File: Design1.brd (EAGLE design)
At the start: 60.6 x 59.4 mm, 24 parts, among them U1 ATMEGA328P-AU, X1 +3.3

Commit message: update
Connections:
- net ESP12F(PIN21) renamed RX
- net ESP12F(PIN22) renamed TX
- net N$5 renamed CH_PD
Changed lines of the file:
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@@
 <?xml version="1.0" encoding="utf-8"?>
 <!DOCTYPE eagle SYSTEM "eagle.dtd">
-<eagle version="8.5.2">
+<eagle version="8.7.1">
 <drawing>
 <settings>
@@
 <wire x1="12.45" y1="19.9754" x2="25.92" y2="14.17" width="0" layer="19" extent="1-1"/>
 </signal>
-<signal name="ESP12F(PIN21)">
+<signal name="RX">
 <contactref element="SJ2" pad="1"/>
 <contactref element="MCU_FIRM2" pad="4"/>
@@
 <wire x1="36.52848125" y1="21.999275" x2="53.592815625" y2="53.58893125" width="0" layer="19" extent="1-16"/>
 </signal>
-<signal name="ESP12F(PIN22)">
+<signal name="TX">
 <contactref element="U1" pad="30"/>
 <contactref element="SJ1" pad="1"/>
@@
 <contactref element="U1" pad="11"/>
 </signal>
-<signal name="N$5">
+<signal name="CH_PD">
 <contactref element="U2" pad="3"/>
 </signal>
@@
 </signal>
 </signals>
-<errors>
-</errors>
 </board>
 </drawing>

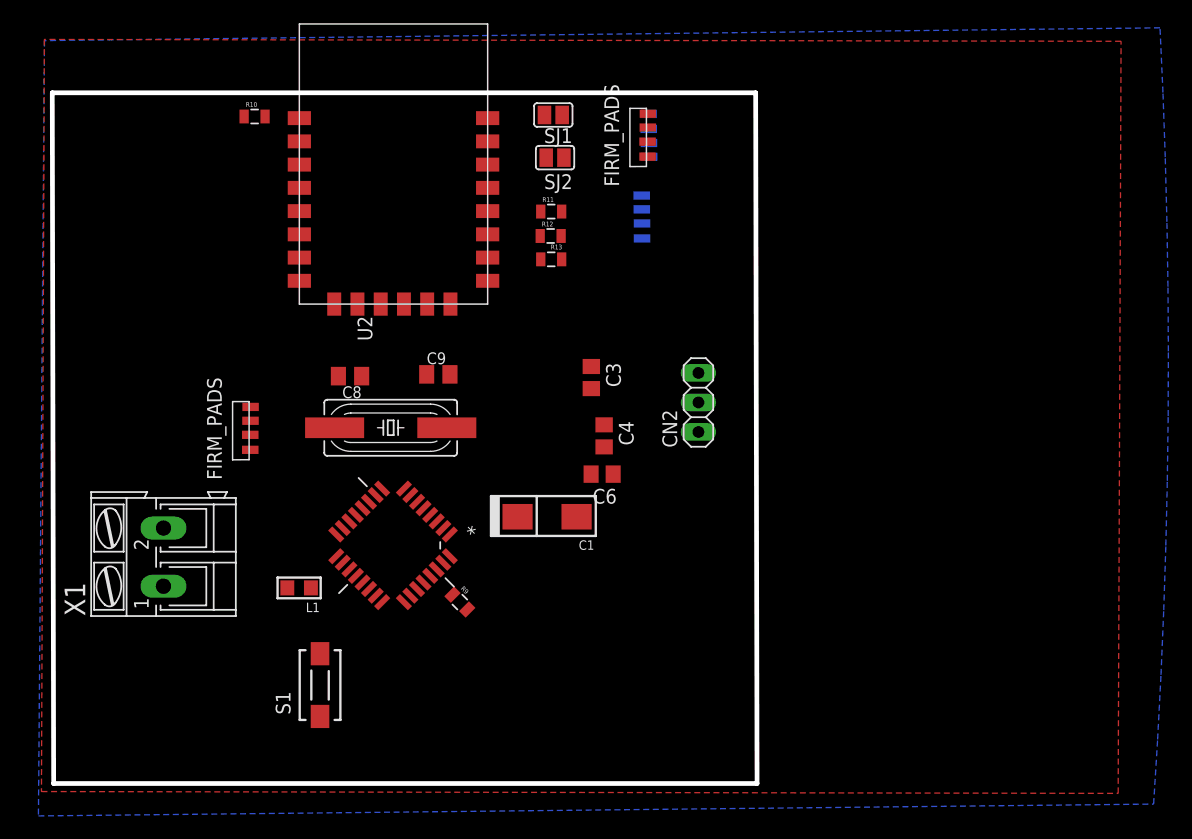
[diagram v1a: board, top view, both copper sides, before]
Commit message: v 0.3 needs location buttons only
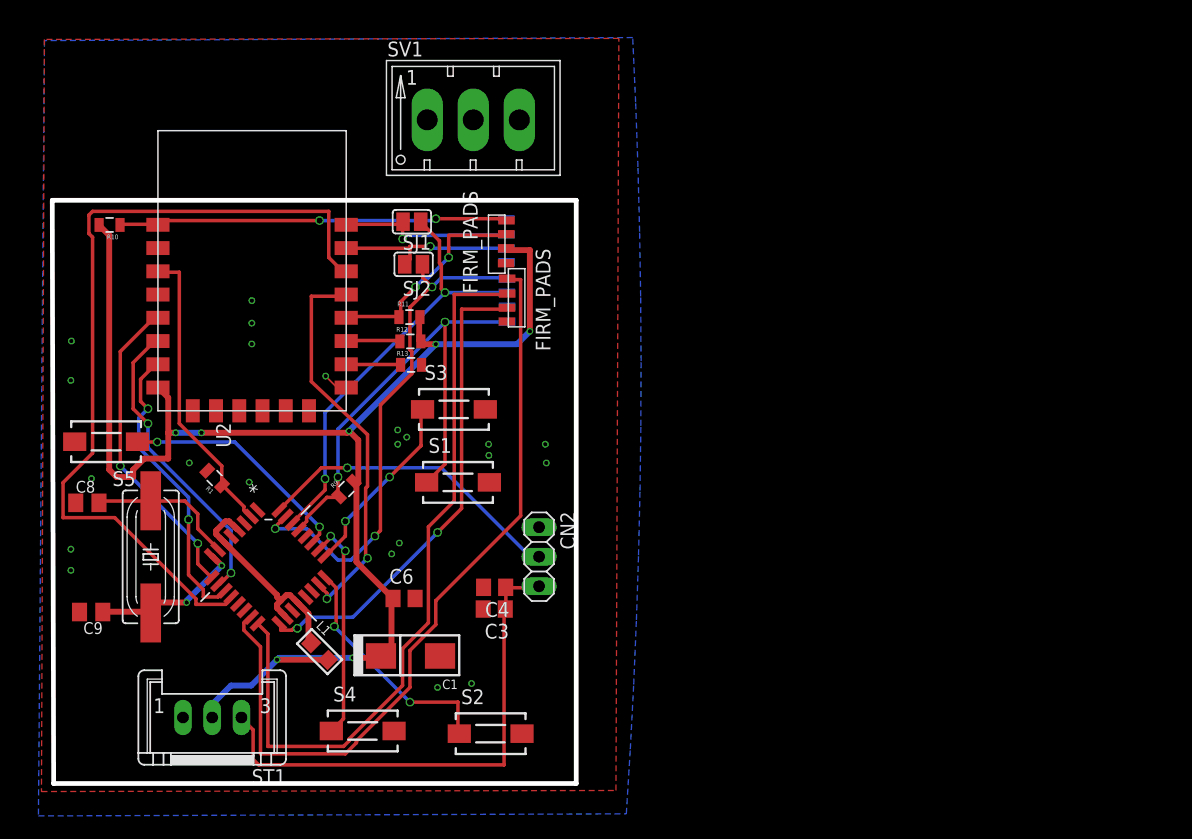
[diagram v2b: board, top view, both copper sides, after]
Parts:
- removed X1: +3.3, con-ptr500:AK300/2
- added R1: 10k, SMD Resistors:0805
- added S2, S3, S4, S5: DTSM-3, switch-tact:DTSM-3
- added ST1: MSF3, con-lumberg:MSF3
- added SV1: (no value), con-amp-mt6:MT6-3Y
- R10: value 10k -> 12K
- moved C9 36.2 mm to (6.22, 17.8), turned to 180 degrees
- moved MCU_FIRM1 27.7 mm to (42.1, 47.3), turned to 270 degrees
- moved C8 25.1 mm to (5.90, 27.1), turned to 0 degrees
- moved OSC1 23.4 mm to (11.3, 22.5), turned to 270 degrees
- moved C3 21.6 mm to (40.9, 18.0), turned to 180 degrees
- moved S1 21.1 mm to (37.8, 28.9), turned to 0 degrees
- moved C6 20.1 mm to (33.1, 18.9), turned to 0 degrees
- moved CN2 19.1 mm to (44.8, 22.5), turned to 270 degrees
- moved C1 16.8 mm to (33.7, 14.0)
- moved C4 16.1 mm to (40.9, 19.9), turned to 180 degrees
- moved R10 15.6 mm to (7.81, 51.1), turned to 180 degrees
- moved U$3 15.3 mm to (41.8, 52.4)
- moved MCU_FIRM3 15.2 mm to (41.8, 46.9)
- moved SJ1 15.2 mm to (33.8, 51.3)
- moved SJ2 15.2 mm to (34.0, 47.7)
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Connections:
- net IRRX renamed MOTION
- removed net +3V1: R9.2
- removed net D/C: U2.13
- removed net N$2: C3.2, C4.2, CN2.1
- removed net RES: U2.14
- removed net SCL: U2.5
- removed net SDA: U2.7
- removed net TEMP: U1.11
- new net 4V5: C3.1, C4.1, CN2.3, ST1.3
- new net BTN_CONFIG: S3.1, U1.25
- new net BTN_RESET: S4.1, U1.26
- new net BTN_TEST: S5.1, U1.27
- new net BTN_UPDATE: S2.1, U1.24
- new net ESP_ACK: U1.12, U2.14
- new net ESP_CONFIG: U1.10, U2.6
- new net ESP_MOTION: U1.9, U2.5
- new net ESP_OK: U1.23, U2.13
- new net ESP_UPDATE: U1.11, U2.7
- new net N$1: MCU_FIRM3.1
- new net N$18: U1.28
- new net N$4: U$3.1
- new net N$8: U1.13
- new net N$9: U1.14
- net +3V3: now also R9.2, ST1.2; no longer C3.1, C4.1, CN2.3, X1.2
- net CH_PD: now also R1.1, U1.2
- net GND: now also C3.2, C4.2, CN2.1, R1.2, S2.2, S3.2, S4.2, S5.2, ST1.1; no longer X1.1
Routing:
- net +3V3: track 0.00 -> 125.5 mm, vias 0 -> 7
- net ESP_ACK: track 0.00 -> 72.1 mm
- net MOSI: track 0.00 -> 68.2 mm
- net MISO: track 0.00 -> 64.9 mm
- net RX: track 0.00 -> 44.8 mm, vias 0 -> 3
- net 4V5: track 0.00 -> 44.0 mm
- net RST_A: track 0.00 -> 43.5 mm, vias 0 -> 2
- net SCK: track 0.00 -> 41.6 mm, vias 0 -> 2
- net TX: track 0.00 -> 37.5 mm, vias 0 -> 2
- net ESP_OK: track 0.00 -> 34.3 mm, vias 0 -> 2
- net RST_E: track 0.00 -> 33.8 mm, vias 0 -> 2
- net ESP_MOTION: track 0.00 -> 27.1 mm, vias 0 -> 2
- net MOTION: track 0.00 -> 27.0 mm, vias 0 -> 1
- net ESP_CONFIG: track 0.00 -> 26.0 mm, vias 0 -> 2
- net ESP_UPDATE: track 0.00 -> 25.9 mm, vias 0 -> 2
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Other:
- board size 60.6 x 59.4 mm -> 45.1 x 50.2 mm

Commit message: v 0.5 good
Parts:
- removed MCU_FIRM1, MCU_FIRM2, MCU_FIRM3, U$3: FIRM_PADSSMD_FIRM_PADS, firm_pads:FIRM_PADS
- added CON1: AT1, firm_pads:FIRM_PADS
- added CON2: AT2, firm_pads:FIRM_PADS
- added CON3: ESP1, firm_pads:FIRM_PADS
- added CON4: ESP2, firm_pads:FIRM_PADS
- S1: value DTSM-3 -> RESET_A
- S2: value DTSM-3 -> UPDATE
- S3: value DTSM-3 -> CONFIG
- S4: value DTSM-3 -> RESET
- S5: value DTSM-3 -> TEST
- moved L1 28.7 mm to (27.5, 43.0), flipped to the bottom, turned to 135 degrees
- moved S3 28.4 mm to (29.3, 7.98)
- moved S5 24.5 mm to (11.0, 8.18)
- moved C9 21.2 mm to (9.08, 38.8), flipped to the bottom, turned to 0 degrees
- moved S2 20.6 mm to (20.0, 8.04)
- moved C1 17.9 mm to (35.3, 31.8), flipped to the bottom, turned to 0 degrees
- moved ST1 16.3 mm to (6.81, 19.2), turned to 90 degrees
- moved U1 14.5 mm to (23.2, 36.0), flipped to the bottom, turned to 135 degrees
- moved S1 14.5 mm to (23.8, 25.2), flipped to the bottom
- moved OSC1 11.8 mm to (14.2, 33.9), flipped to the bottom, turned to 90 degrees
- moved S4 9.06 mm to (38.6, 7.88)
- moved C6 8.63 mm to (35.5, 27.2), flipped to the bottom, turned to 180 degrees
- moved C8 4.10 mm to (9.49, 29.1), flipped to the bottom, turned to 180 degrees
- moved R1 2.28 mm to (19.1, 29.2), flipped to the bottom, turned to 315 degrees
- moved R9 1.62 mm to (28.5, 29.9), flipped to the bottom, turned to 225 degrees
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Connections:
- net N$11 renamed AT_VCC
- removed net N$1: MCU_FIRM3.1
- removed net N$17: MCU_FIRM1.4
- net +3V3: now also CON3.2; no longer MCU_FIRM3.2
- net CH_PD: now also CON3.1
- net GND: now also CON1.4, CON4.4; no longer MCU_FIRM2.2, U$3.4
- net GPIO0: now also CON3.3; no longer MCU_FIRM3.3
- net MISO: now also CON1.2; no longer MCU_FIRM1.2
- net MOSI: now also CON1.1; no longer MCU_FIRM1.1
- net N$4: now also CON4.1; no longer U$3.1
- net RST_A: now also CON2.1; no longer MCU_FIRM2.1
- net RST_E: now also CON3.4; no longer MCU_FIRM3.4
- net RX: now also CON2.4; no longer MCU_FIRM2.4
- net RXD_FIRM: now also CON4.2; no longer U$3.2
- net SCK: now also CON1.3; no longer MCU_FIRM1.3
- net TX: now also CON2.3; no longer MCU_FIRM2.3
- net TXD_FIRM: now also CON4.3; no longer U$3.3
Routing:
- net ESP_ACK: track 72.1 -> 13.3 mm, vias 0 -> 1
- net CH_PD: track 25.5 -> 73.7 mm, vias 0 -> 3
- net MISO: track 64.9 -> 27.4 mm
- net MOSI: track 68.2 -> 31.7 mm, vias 0 -> 2
- net BTN_UPDATE: track 20.8 -> 56.4 mm, vias 2 -> 1
- net SCK: track 41.6 -> 20.8 mm, vias 2 -> 0
- net RST_A: track 43.5 -> 60.1 mm
- net ESP_UPDATE: track 25.9 -> 9.41 mm, vias 2 -> 1
- net ESP_CONFIG: track 26.0 -> 9.77 mm, vias 2 -> 1
- net BTN_TEST: track 20.3 -> 34.2 mm, vias 2 -> 1
- net RX: track 44.8 -> 58.2 mm
- net ESP_OK: track 34.3 -> 21.1 mm, vias 2 -> 1
- net ESP_MOTION: track 27.1 -> 14.3 mm, vias 2 -> 1
- net BTN_CONFIG: track 16.1 -> 28.8 mm, vias 2 -> 1
- net BTN_RESET: track 19.4 -> 30.5 mm, vias 2 -> 1
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
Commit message: v0.6
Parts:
- removed SV1: (no value), con-amp-mt6:MT6-3Y
- added BAT: Bat, jumper:SJ
- added BATL3.3: 3.3, jumper:SJ
- added BATL4.5: 4.5, jumper:SJ
- added CN1: (no value), MicroUSB:USB-MICRO-SMD
- added SG1: F/CM12P, buzzer:F/CM12P
- added U3: LDO, SPX3819M5-L-3-3:SOT95P280X145-5N
- S1, S2, S3, S4, S5: device switch-tact:DTSM-3 -> switch-tact:DTSM-6
- moved S1 21.2 mm to (41.2, 37.3), turned to 180 degrees
- moved S2 20.2 mm to (40.1, 8.79)
- moved C1 15.0 mm to (28.6, 18.3), turned to 270 degrees
- moved S3 14.0 mm to (31.2, 21.9)
- moved S4 9.71 mm to (29.0, 9.00)
- moved C6 8.83 mm to (33.9, 18.5), turned to 90 degrees
- moved S5 7.18 mm to (18.1, 8.99), turned to 0 degrees
- moved ST1 3.56 mm to (4.19, 21.6)
- moved R1 3.54 mm to (22.2, 31.0), turned to 45 degrees
- moved L1 3.27 mm to (30.7, 43.7)
- moved U1 3.13 mm to (26.3, 36.0)
- moved C8 2.94 mm to (12.4, 29.6)
- moved C9 2.84 mm to (11.8, 38.1)
- moved OSC1 2.64 mm to (16.8, 33.5)
- moved R9 2.58 mm to (31.0, 30.5)
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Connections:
- net N$9 renamed SS-
- removed net N$8: U1.13
- new net BAT: BAT.2, BATL3.3.1, ST1.2
- new net BUZZER: SG1.+, U1.13
- new net N$1: BATL3.3.2, BATL4.5.2, CN1.VBUS1, U3.1, U3.3
- net +3V3: now also BAT.1, U3.5; no longer ST1.2
- net 4V5: now also BATL4.5.1
- net GND: now also CN1.GND1, S1.3, S2.3, S3.3, S4.3, S5.3, SG1.-, U3.2; no longer S1.2, S2.2, S3.2, S4.2, S5.2
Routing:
- net BUZZER: track 0.00 -> 83.5 mm, vias 0 -> 1
- net RST_A: track 60.1 -> 27.3 mm, vias 2 -> 0
- net BTN_UPDATE: track 56.4 -> 28.0 mm
- net N$1: track 0.00 -> 25.6 mm, vias 0 -> 2
- net BTN_CONFIG: track 28.8 -> 13.2 mm
- net 4V5: track 40.0 -> 53.5 mm
- net BAT: track 0.00 -> 10.8 mm
- net MOSI: track 31.7 -> 21.5 mm, vias 2 -> 0
- net RX: track 58.2 -> 49.0 mm, vias 3 -> 4
- net MISO: track 27.4 -> 19.4 mm
- net GND: track 0.00 -> 5.97 mm, vias 20 -> 15
- net TX: track 44.1 -> 38.3 mm
- net ESP_UPDATE: track 9.41 -> 13.2 mm
- net SCK: track 20.8 -> 17.1 mm
- net ESP_OK: track 21.1 -> 17.7 mm
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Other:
- board size 45.1 x 50.2 mm -> 45.4 x 50.4 mm

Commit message: v 0.6 Add some notes
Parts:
- moved BATL4.5 0.70 mm to (14.2, 16.8)
- moved R1 0.51 mm to (21.7, 30.7)
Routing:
- net 4V5: track 53.5 -> 55.0 mm
- net CH_PD: track 76.2 -> 77.1 mm
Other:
- board size 45.4 x 50.4 mm -> 45.9 x 50.5 mm
- board text added: "1"
- board text added: "3.3V [2.2:3.6]v"
- board text added: "4.5V [3:10]v"
- board text added: "GND"
- board text added: "RST_E GPIO0 3.3 CH_PD NC RX TX GND"
- board text added: "RX TX NC REST_A MOSI MISO SCK GND"
